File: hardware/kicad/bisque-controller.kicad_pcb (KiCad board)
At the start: 2 copper layers, 100 x 80 mm, 49 parts, among them J1 USB-C, J2 5V_IN, J3 TC_K, J4 SSR, J5 DISPLAY, J6 NAV_SW, J7 AUX, Q1 AO3400A, Q2 AO3400A, SW1 RESET, SW2 BOOT, U1 ESP32-S3-WROOM-1-N8R2, U2 AMS1117-3.3, U3 MAX31855KASA+, U4 USBLC6-2SC6

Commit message: Replace pin headers with Molex KK-254 friction-lock headers
J5 (display), J6 (nav switch) and J7 (aux) switch from plain 2.54mm pin
headers to Molex KK-254 AE-6410 friction-lock headers, so each mating
housing is polarized and cannot be plugged in reversed. Pin positions are
unchanged (same 2.54mm row); the board was re-routed around the larger
oval pads and re-verified (ALL CHECKS PASS). Silk pin-name labels moved
out from under the deeper connector bodies, 3D renders updated with the
friction-lock body shape, BOM lists the headers plus mating housings and
crimp terminals.

Co-Authored-By: Claude Fable 5 <noreply@anthropic.com>
Claude-Session: https://claude.ai/code/session_017JbapEYPC7fC91erkTARYt
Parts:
- J5, J7: footprint Connector_PinHeader_2.54mm:PinHeader_1x08_P2.54mm_Vertical -> Connector_Molex:Molex_KK-254_AE-6410-08A_1x08_P2.54mm_Vertical
- J6: footprint Connector_PinHeader_2.54mm:PinHeader_1x06_P2.54mm_Vertical -> Connector_Molex:Molex_KK-254_AE-6410-06A_1x06_P2.54mm_Vertical
- turned J5 to 0 degrees
- turned J6 to 0 degrees
- turned J7 to 0 degrees
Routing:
- net LCD_RST: track 105.8 -> 100.2 mm, vias 4 -> 5
- net LCD_DC: track 98.5 -> 104.1 mm, vias 5 -> 4
- net LID_SW: track 64.9 -> 65.7 mm
- net LCD_BL: track 91.0 -> 91.8 mm
- net GND: vias 107 -> 104

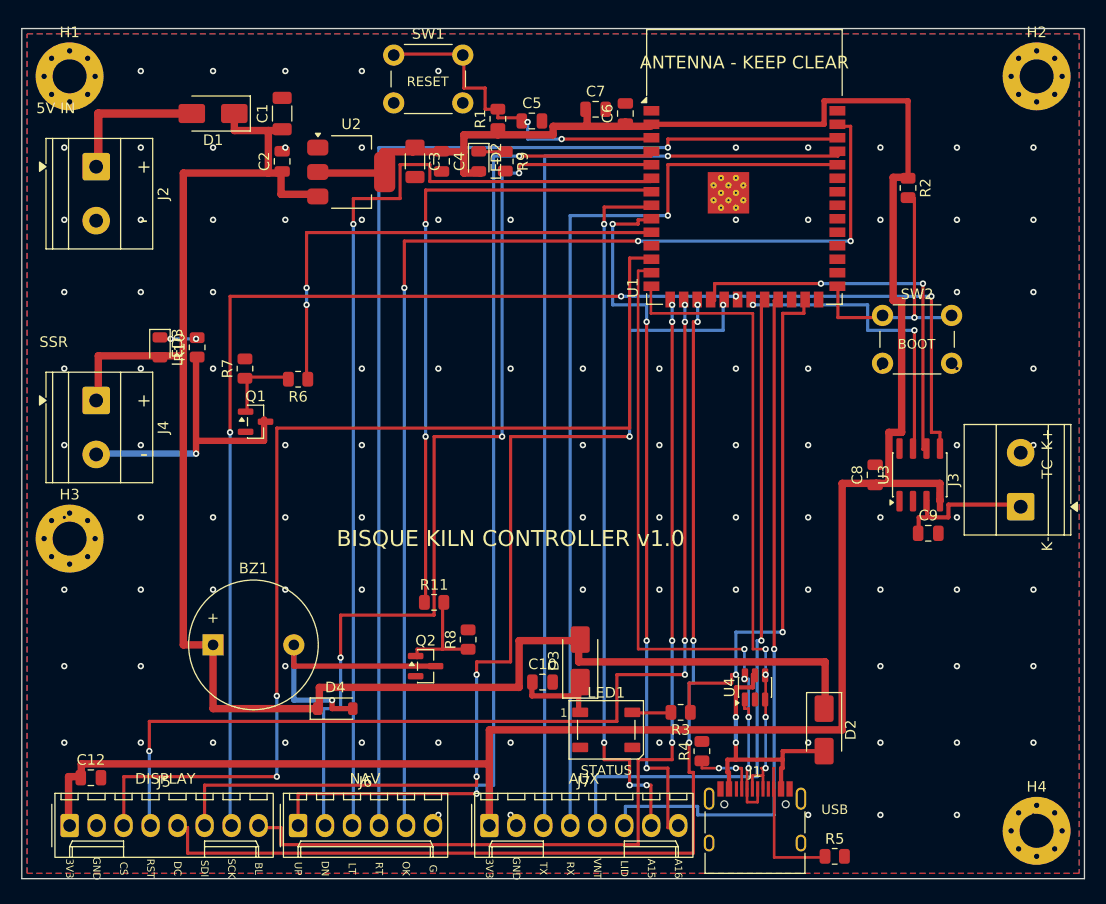
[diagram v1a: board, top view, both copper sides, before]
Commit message: Re-route board with octilinear (45-degree) routing
Upgrade the grid autorouter from 4-direction Manhattan to 8-direction
octilinear A*: diagonal moves with octile heuristic, corner-clip
protection (a diagonal step requires both adjacent orthogonal cells to be
free), and graded bend costs (45-degree turns cheap, 90-degree turns
expensive, reversals effectively forbidden) so traces come out straight
or gently mitred instead of stair-stepped. A post-pass chamfers any
remaining right-angle corners into 45-degree miters, each validated
against the full obstacle model before being applied.

This follows standard PCB layout practice: 45-degree corners avoid the
acid-trap/over-etch risk of sharp 90s, shorten the electrical path, and
reduce impedance discontinuity at bends. Re-verified: ALL CHECKS PASS
(clearance >= 0.2 mm, connectivity, antenna keepout, edge, courtyards).
2D preview and 3D renders regenerated.

Co-Authored-By: Claude Fable 5 <noreply@anthropic.com>
Claude-Session: https://claude.ai/code/session_017JbapEYPC7fC91erkTARYt
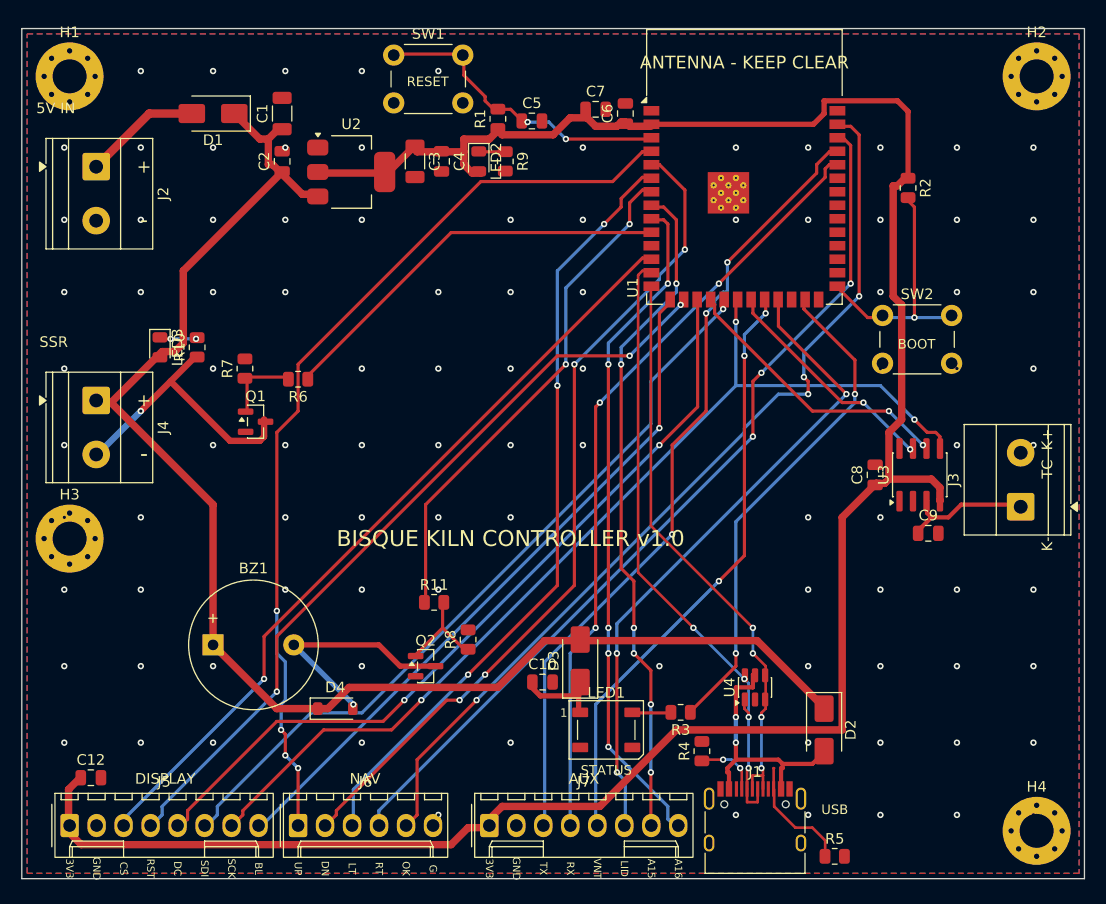
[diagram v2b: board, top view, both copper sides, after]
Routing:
- net SPI_SCLK: track 131.9 -> 95.7 mm, vias 4 -> 3
- net LCD_CS: track 103.3 -> 74.7 mm, vias 2 -> 1
- net LCD_DC: track 104.1 -> 75.8 mm, vias 4 -> 2
- net LCD_BL: track 91.8 -> 65.9 mm, vias 4 -> 1
- net SPI_MOSI: track 98.5 -> 72.8 mm, vias 4 -> 1
- net LCD_RST: track 100.2 -> 74.6 mm, vias 5 -> 3
- net +5V: track 162.1 -> 137.6 mm
- net BTN_RIGHT: track 108.1 -> 84.2 mm, vias 1 -> 3
- net BTN_SEL: track 109.4 -> 87.4 mm, vias 3 -> 4
- net BTN_LEFT: track 92.5 -> 73.4 mm, vias 1 -> 3
- net TXD0: track 91.3 -> 75.8 mm, vias 1 -> 3
- net RXD0: track 87.7 -> 73.4 mm, vias 1 -> 3
- net BTN_DOWN: track 93.3 -> 79.0 mm, vias 3 -> 4
- net ALARM: track 60.2 -> 48.2 mm
- net +3V3: track 232.1 -> 220.4 mm
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
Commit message: Verify JLCPCB manufacturability, add assembly BOM/CPL export
- Confirm the board clears JLCPCB standard 2-layer capabilities with wide
  margins (0.25mm min track vs 0.127 limit, 0.6/0.3 vias, 0.3mm min
  drill, 100x80mm inside the cheapest <=100x100mm tier) — no upcharges.
- Fix U1 variant: firmware sdkconfig uses octal PSRAM and a 16MB OTA
  partition table, so the module must be ESP32-S3-WROOM-1-N16R8 (LCSC
  C2913202, in stock), not N8R2. IO35-37 were already NC on the board as
  octal PSRAM requires.
- Consolidate C1/C3 to one 22uF/25V 1206 part for BOM simplicity.
- New generator/gen_jlc.py emits jlcpcb/BOM.csv + CPL.csv with LCSC part
  numbers (verified ones marked; commodity parts flagged for confirmation
  in JLC's BOM matcher). Key parts verified in catalog: ESP32-S3 module,
  MAX31855KASA+T (C52028), USB-C TYPE-C-31-M-12 (C165948), AMS1117,
  AO3400A, SS34/SS14, 1N4148W and all passives as Basic parts.
- README: fabrication capability table, price expectations, and three
  assembly strategies (SMT-only recommended).

Co-Authored-By: Claude Fable 5 <noreply@anthropic.com>
Claude-Session: https://claude.ai/code/session_017JbapEYPC7fC91erkTARYt
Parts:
- C3: value 22uF/10V -> 22uF/25V
- U1: value ESP32-S3-WROOM-1-N8R2 -> ESP32-S3-WROOM-1-N16R8
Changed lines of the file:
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@@
 			)
 		)
-		(property "Value" "ESP32-S3-WROOM-1-N8R2"
+		(property "Value" "ESP32-S3-WROOM-1-N16R8"
 			(at 0 14.6 0)
 			(unlocked yes)
@@
 			)
 		)
-		(property "Value" "22uF/10V"
+		(property "Value" "22uF/25V"
 			(at 0 1.85 270)
 			(layer "F.Fab")

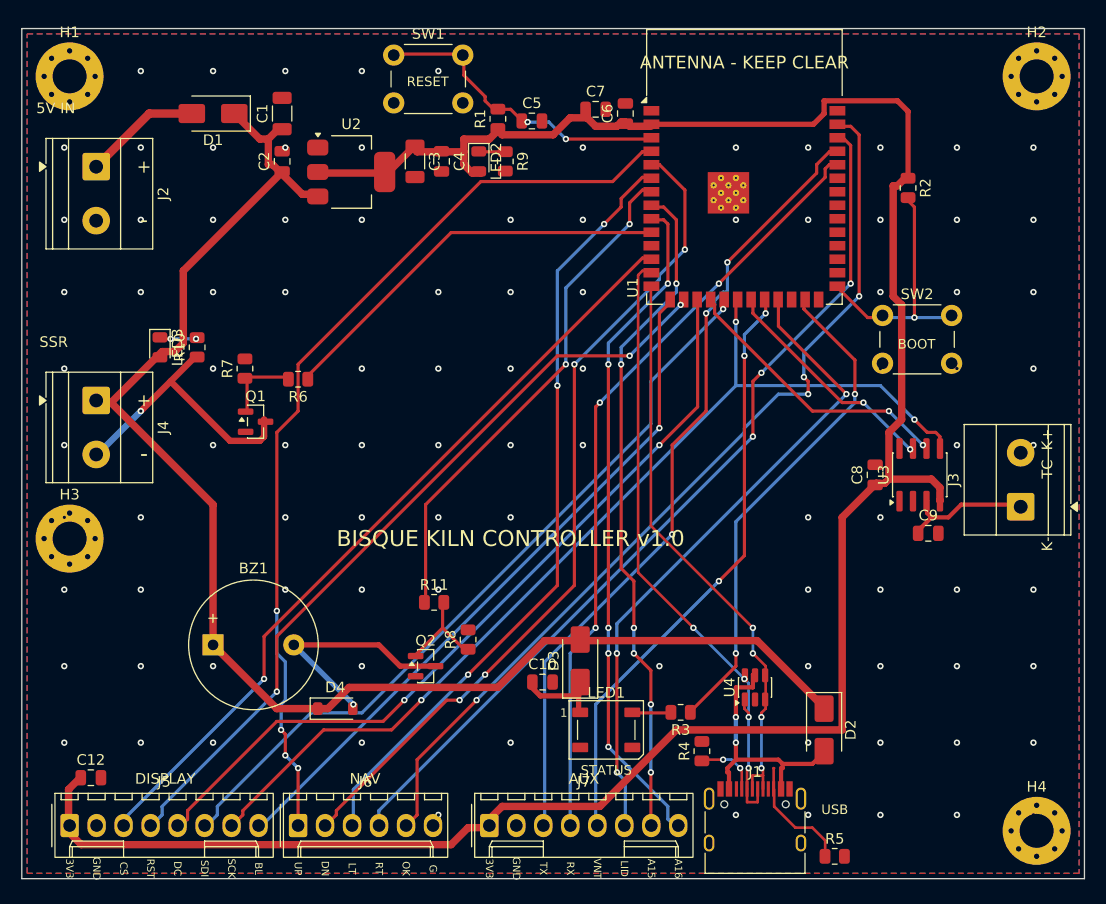
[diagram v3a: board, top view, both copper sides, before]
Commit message: Rebuild PCB and schematic through real KiCad (7.0.11)
KiCad is now installed in the build environment (Ubuntu universe; the
KiCad 9 PPA is blocked by network policy), so the project is rebuilt
through KiCad's own engine instead of hand-written file generation:

- generator/kicad_build.py constructs the board via the pcbnew Python
  API: footprints loaded from KiCad's installed system libraries, router
  obstacle model taken from the loaded pad geometry, tracks/vias/zones/
  silk added as real pcbnew objects, ground pours filled by KiCad's
  ZONE_FILLER, saved by pcbnew (KiCad 7 format, opens in 7/8/9).
- KiCad DRC (WriteDRCReport) runs as part of the build: ZERO errors,
  zero unconnected items (report committed). DRC drove real fixes my
  own checker had missed: module EP thermal vias upsized 0.2->0.3mm
  (keeps JLCPCB standard drill range), hole-to-hole clearance added to
  the router's via placement, solid pour connections where thermal
  spokes starved, explicit GND stubs routed for every SMD GND pad plus
  automatic pour-island healing (stitch via dropped into any isolated
  fill fragment), and a pre-seeded escape for U4's boxed-in GND pin.
- Schematic regenerated in KiCad 7 format from the system symbol
  libraries and validated by round-trip: kicad-cli exports the netlist
  and check_netlist.py diffs it against design.py - 42 nets, 0
  mismatches.
- Fabrication outputs exported with kicad-cli and committed: gerbers +
  Excellon drill + job file (gerbers/), schematic + board PDFs (pdf/).
- .kicad_pro rewritten by pcbnew as a native project with full rule
  severities; 2D/3D previews regenerated; README workflow updated.
  gen_pcb.py retained as a KiCad-free fallback generator.

Co-Authored-By: Claude Fable 5 <noreply@anthropic.com>
Claude-Session: https://claude.ai/code/session_017JbapEYPC7fC91erkTARYt
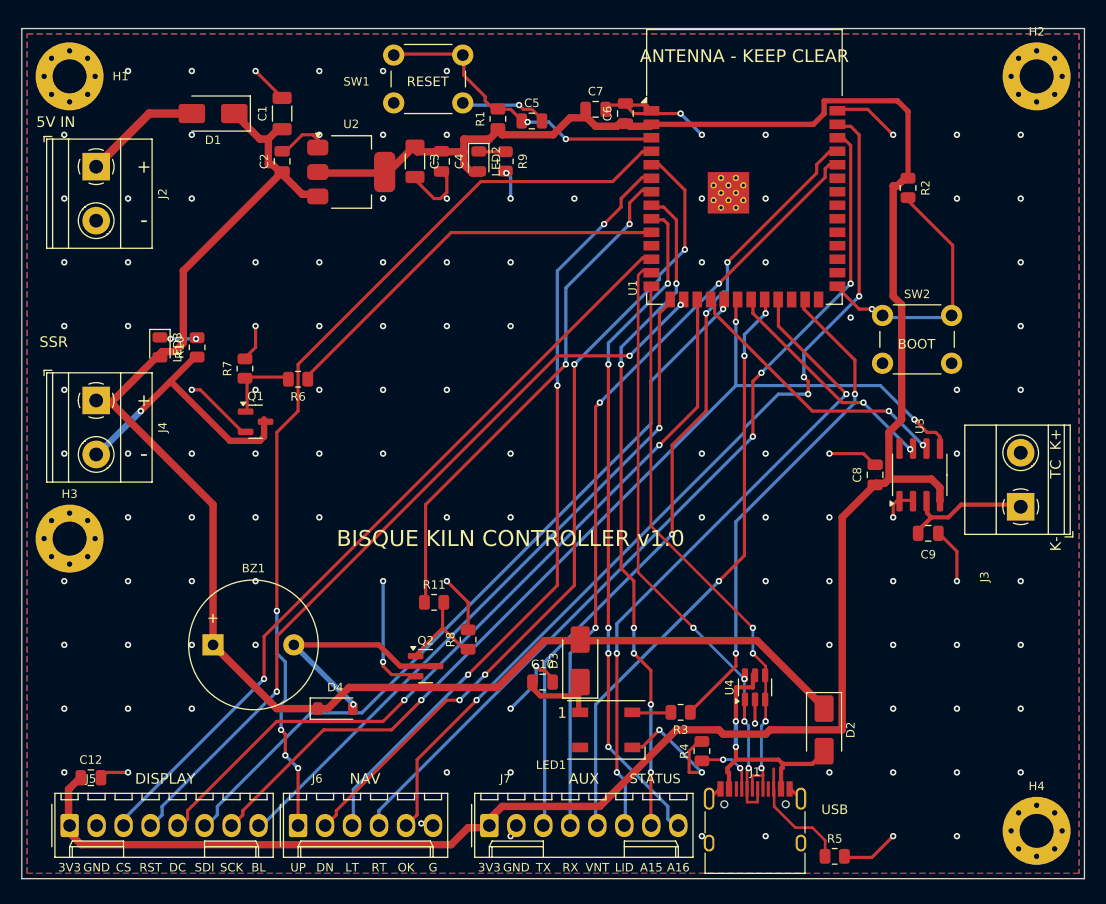
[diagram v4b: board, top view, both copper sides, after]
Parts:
- BZ1: footprint Buzzer_Beeper:Buzzer_12x9.5RM7.6 -> Buzzer_12x9.5RM7.6
- C1, C3: footprint Capacitor_SMD:C_1206_3216Metric -> C_1206_3216Metric
- C10, C12, C2, C4, C5, C6, C7, C8, C9: footprint Capacitor_SMD:C_0805_2012Metric -> C_0805_2012Metric
- D1, D2, D3: footprint Diode_SMD:D_SMA -> D_SMA
- D4: footprint Diode_SMD:D_SOD-123 -> D_SOD-123
- H1, H2, H3, H4: footprint MountingHole:MountingHole_3.2mm_M3_Pad_Via -> MountingHole_3.2mm_M3_Pad_Via
- J1: footprint Connector_USB:USB_C_Receptacle_HRO_TYPE-C-31-M-12 -> USB_C_Receptacle_HRO_TYPE-C-31-M-12
- J2, J3, J4: footprint TerminalBlock_Phoenix:TerminalBlock_Phoenix_MKDS-1,5-2-5.08_1x02_P5.08mm_Horizontal -> TerminalBlock_Phoenix_MKDS-1,5-2-5.08_1x02_P5.08mm_Horizontal
- J5, J7: footprint Connector_Molex:Molex_KK-254_AE-6410-08A_1x08_P2.54mm_Vertical -> Molex_KK-254_AE-6410-08A_1x08_P2.54mm_Vertical
- J6: footprint Connector_Molex:Molex_KK-254_AE-6410-06A_1x06_P2.54mm_Vertical -> Molex_KK-254_AE-6410-06A_1x06_P2.54mm_Vertical
- LED1: footprint LED_SMD:LED_WS2812B_PLCC4_5.0x5.0mm_P3.2mm -> LED_WS2812B_PLCC4_5.0x5.0mm_P3.2mm
- LED2, LED3: footprint LED_SMD:LED_0805_2012Metric -> LED_0805_2012Metric
- Q1, Q2: footprint Package_TO_SOT_SMD:SOT-23 -> SOT-23
- R1, R10, R11, R2, R3, R4, R5, R6, R7, R8, R9: footprint Resistor_SMD:R_0805_2012Metric -> R_0805_2012Metric
- SW1, SW2: footprint Button_Switch_THT:SW_PUSH_6mm -> SW_PUSH_6mm
- U1: footprint RF_Module:ESP32-S3-WROOM-1 -> ESP32-S3-WROOM-1
- U2: footprint Package_TO_SOT_SMD:SOT-223-3_TabPin2 -> SOT-223-3_TabPin2
- U3: footprint Package_SO:SOIC-8_3.9x4.9mm_P1.27mm -> SOIC-8_3.9x4.9mm_P1.27mm
- U4: footprint Package_TO_SOT_SMD:SOT-23-6 -> SOT-23-6
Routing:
- net GND: track 0.00 -> 123.5 mm, vias 99 -> 123
- net IO0: track 24.1 -> 25.6 mm
- net EN: track 29.2 -> 28.7 mm

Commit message: Rebuild board with local KiCad 10.0.4; raytraced renders via kicad-cli
Recreates the PCB and all outputs with the locally installed KiCad 10:

- kicad_build.py is now version-adaptive: on KiCad 8+ the board is built
  via the pcbnew API, saved, then kicad-cli pcb drc --refill-zones
  --save-board fills the pours and runs DRC in one authentic pass (the
  v7 in-memory flow is kept for that generation). macOS standalone
  scripting fixes: wx.App bootstrap, PCB_IO_MGR.FindPlugin footprint
  loading, EDA_UNITS_MM, SetLocalZoneConnection.
- KiCad 10 library rename handled: the USB-C shield pin/pads are 'SH'
  (was 'S1' in <=9); design.py carries both aliases and the netlist
  round-trip normalizes them. Round-trip: 42 nets, 0 mismatches.
- KiCad 10 DRC: 0 errors, 0 unconnected, 16 cosmetic silk warnings
  (report committed). Independent geometry checker updated for the v10
  file format (name-referenced nets) - ALL CHECKS PASS.
- 3D renders are now genuine kicad-cli raytraces with official component
  models (generator/render-3d.sh); the three.js renderer remains as a
  KiCad-free fallback. Gerbers/drill/PDFs re-exported with kicad-cli 10.

Co-Authored-By: Claude Fable 5 <noreply@anthropic.com>
Claude-Session: https://claude.ai/code/session_017JbapEYPC7fC91erkTARYt
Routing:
- net IO0: track 25.6 -> 24.1 mm
- net EN: track 28.7 -> 29.2 mm
- net GND: vias 123 -> 122
